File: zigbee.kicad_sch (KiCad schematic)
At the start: 17 parts, among them IC2 CC2652P1FRGZR, Y1 Crystal, Y2 Crystal_GND24

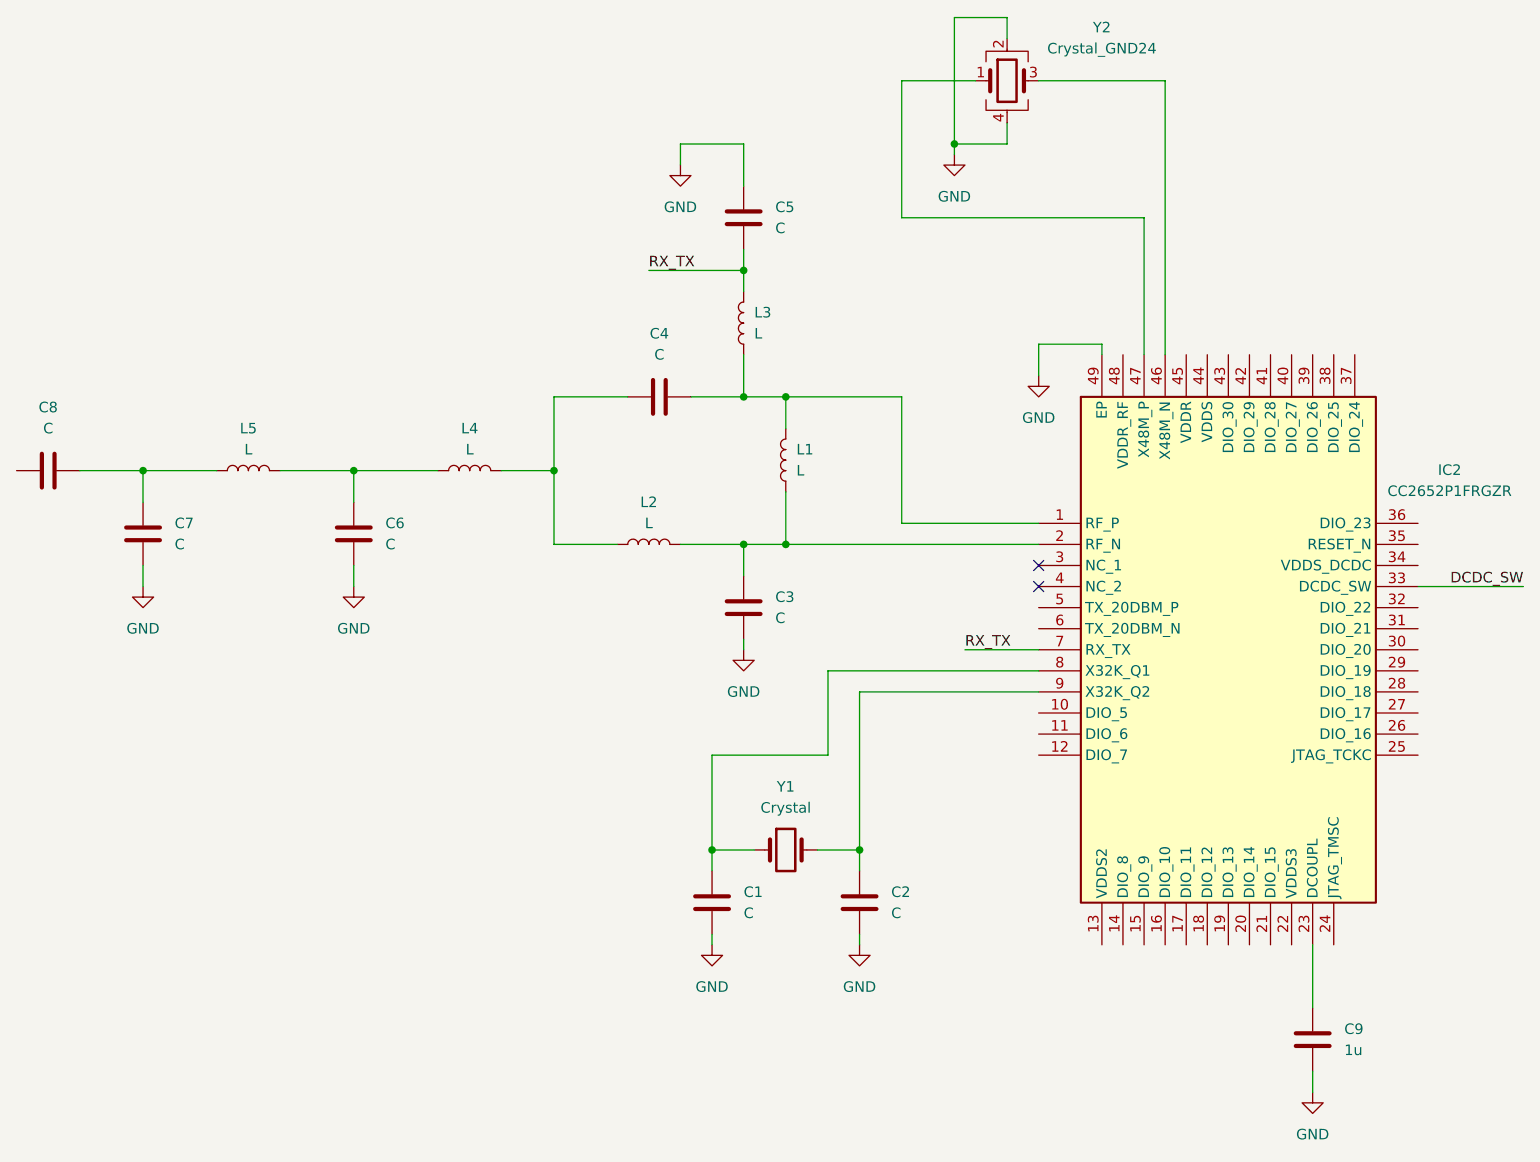
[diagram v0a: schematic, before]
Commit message: Started power circuitry and added more custom schematic symbols
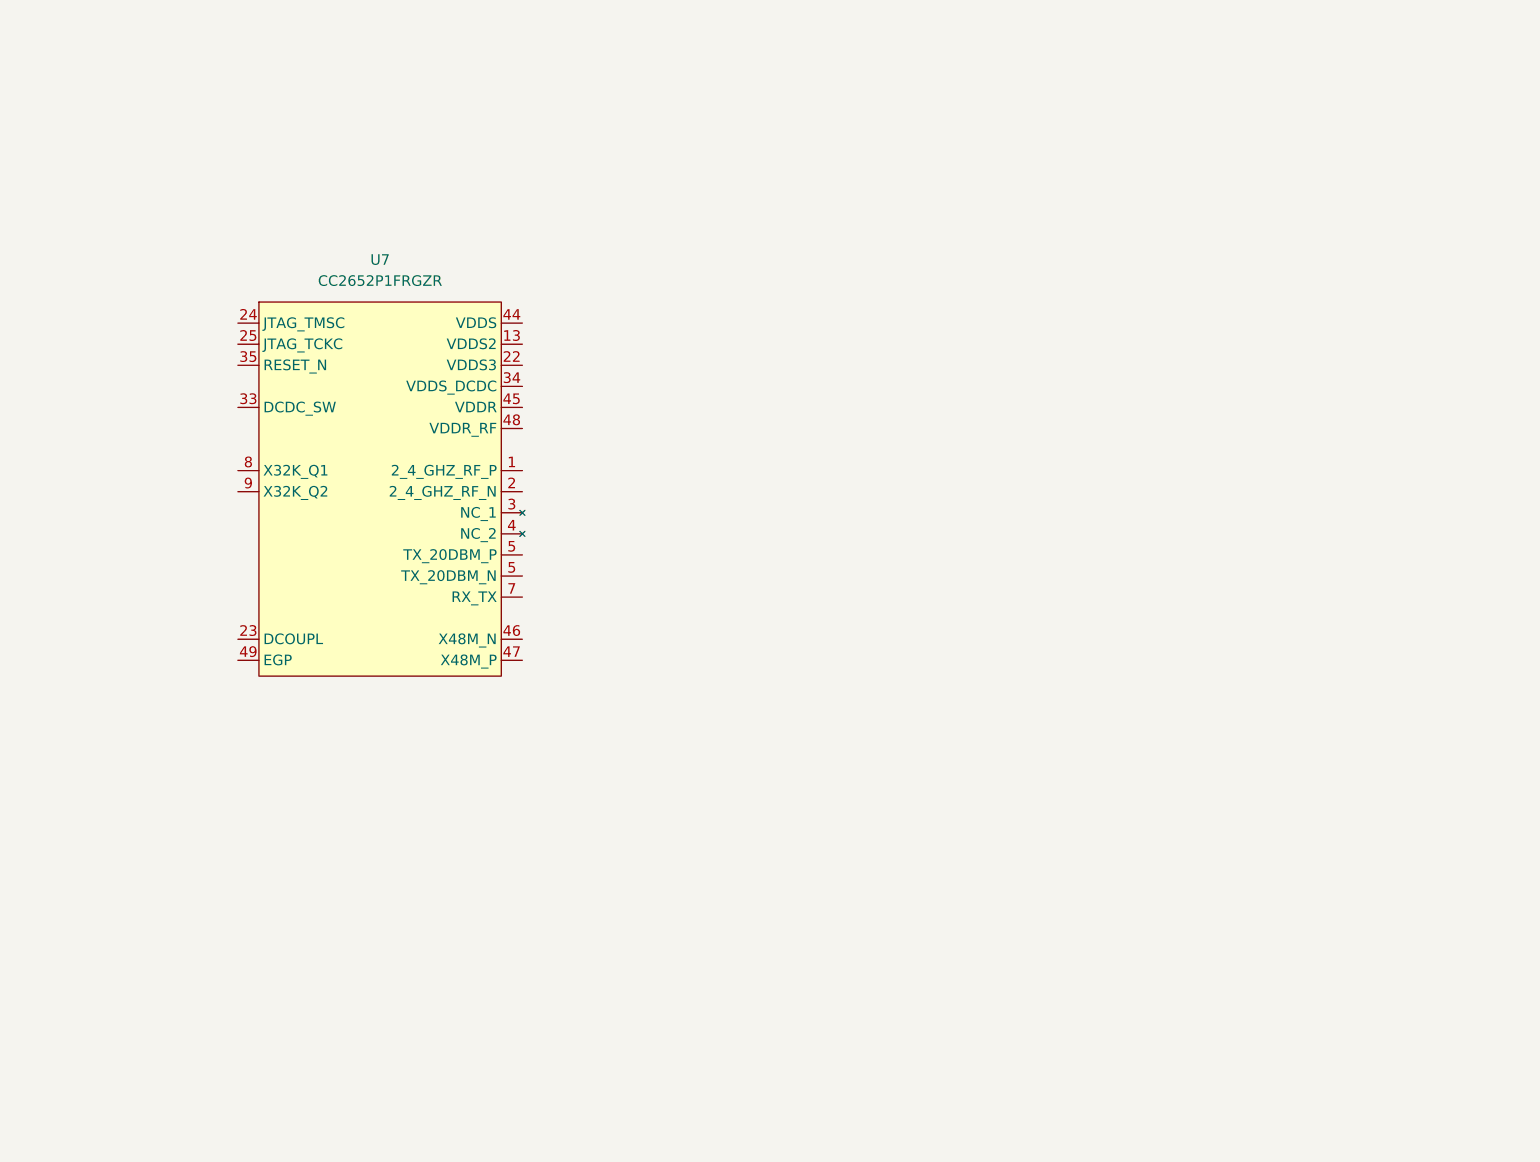
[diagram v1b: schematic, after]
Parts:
- removed C1, C2, C3, C4, C5, C6, C7, C8: C, symbol Device:C
- removed C9: 1u, symbol Device:C
- removed IC2: CC2652P1FRGZR, CC2652P1FRGZR:QFN50P700X700X100-49N-D, symbol CC2652P1FRGZR:CC2652P1FRGZR
- removed L1, L2, L3, L4, L5: L, symbol Device:L
- removed Y1: Crystal, symbol Device:Crystal
- removed Y2: Crystal_GND24, symbol Device:Crystal_GND24
- added U7: CC2652P1FRGZR, symbol SoftServicesSymbolLibrary:CC2652P1FRGZR
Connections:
- no-connect marks 2 -> 0

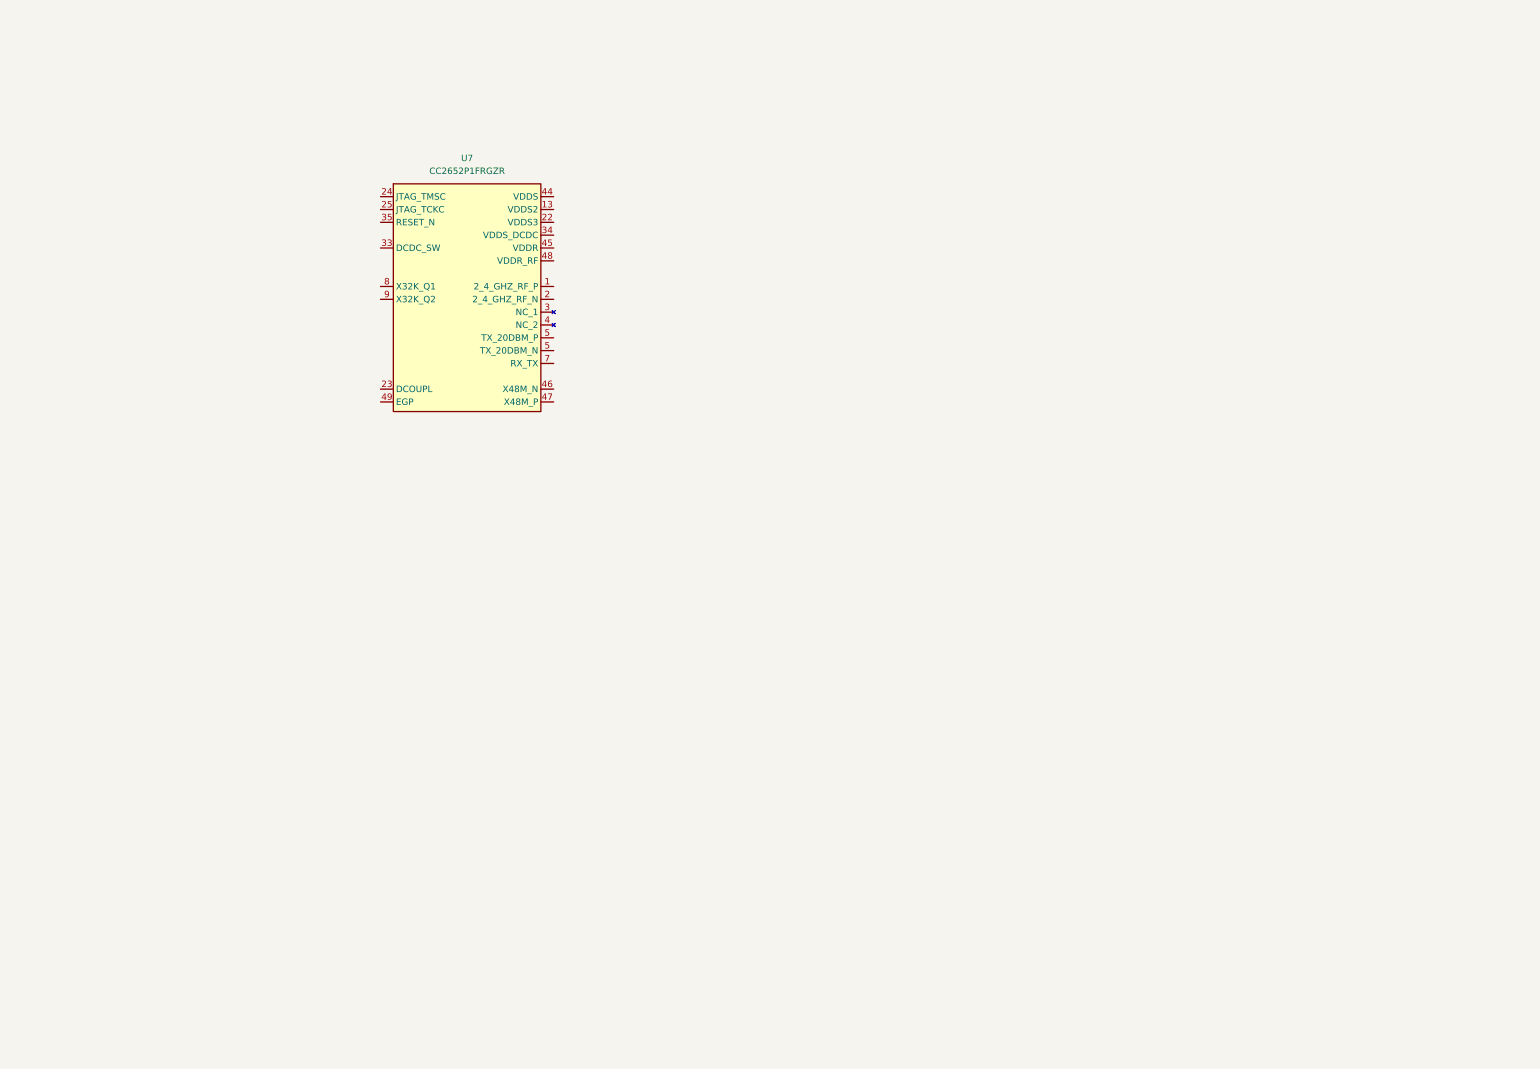
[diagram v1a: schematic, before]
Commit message: Finished CC2652P schematic
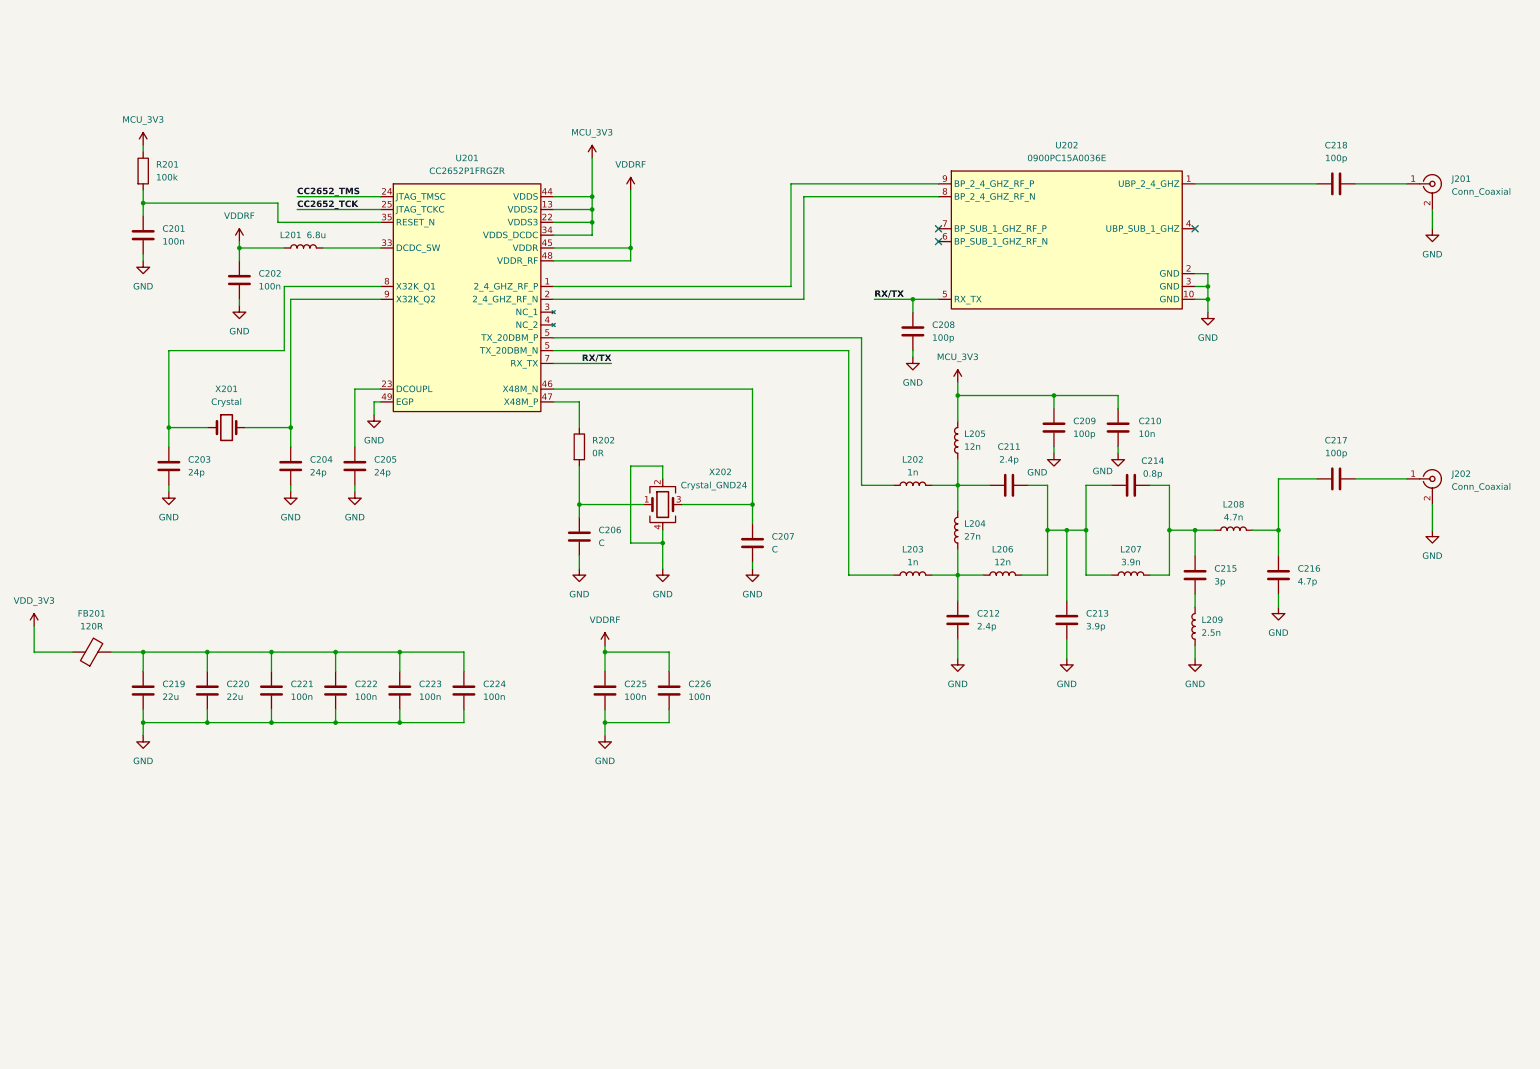
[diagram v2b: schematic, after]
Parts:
- added C201, C202, C221, C222, C223, C224, C225, C226: 100n, symbol Device:C
- added C203, C204, C205: 24p, symbol Device:C
- added C206, C207: C, symbol Device:C
- added C208, C209, C217, C218: 100p, symbol Device:C
- added C210: 10n, symbol Device:C
- added C211, C212: 2.4p, symbol Device:C
- added C213: 3.9p, symbol Device:C
- added C214: 0.8p, symbol Device:C
- added C215: 3p, symbol Device:C
- added C216: 4.7p, symbol Device:C
- added C219, C220: 22u, symbol Device:C
- added FB201: 120R, symbol Device:FerriteBead
- added J201, J202: Conn_Coaxial, symbol Connector:Conn_Coaxial
- added L201: 6.8u, symbol Device:L
- added L202, L203: 1n, symbol Device:L
- added L204: 27n, symbol Device:L
- added L205, L206: 12n, symbol Device:L
- added L207: 3.9n, symbol Device:L
- added L208: 4.7n, symbol Device:L
- added L209: 2.5n, symbol Device:L
- added R201: 100k, symbol Device:R
- added R202: 0R, symbol Device:R
- added U202: 0900PC15A0036E, symbol SoftServicesSymbolLibrary:0900PC15A0036E
- added X201: Crystal, symbol Device:Crystal
- added X202: Crystal_GND24, symbol Device:Crystal_GND24
- renumbered U7 to U201
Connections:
- net at U201.1 (2_4_GHZ_RF_P): now also U202.9 (BP_2_4_GHZ_RF_P)
- net MCU_3V3: now reaches U201.13 (VDDS2)
- net MCU_3V3: now also U201.22 (VDDS3), U201.34 (VDDS_DCDC), U201.44 (VDDS), C209.1, C210.1, L205.2, R201.1
- net at U201.2 (2_4_GHZ_RF_N): now also U202.8 (BP_2_4_GHZ_RF_N)
- net at U201.23 (DCOUPL): now also C205.1
- net CC2652_TMS: now reaches U201.24 (JTAG_TMSC)
- net CC2652_TCK: now reaches U201.25 (JTAG_TCKC)
- net at U201.33 (DCDC_SW): now also L201.2
- net at U201.35 (RESET_N): now also C201.1, R201.2
- net VDDRF: now reaches U201.45 (VDDR)
- net VDDRF: now also U201.48 (VDDR_RF), C202.1, C225.1, C226.1, L201.1
- net at U201.46 (X48M_N): now also C207.1, X202.3
- net at U201.47 (X48M_P): now also R202.1
- net GND: now reaches U201.49 (EGP)
- net GND: now also C201.2, C202.2, C203.2, C204.2, C205.2, C206.2, C207.2, C208.2, C209.2, C210.2, C212.2, C213.2, C216.1, C219.2, C220.2, C221.2, C222.2, C223.2, C224.2, C225.2, C226.2, J201.2 (Ext), J202.2 (Ext), L209.1, U202.10 (GND), U202.2 (GND), U202.3 (GND), X202.2, X202.4
- net at U201.5 (TX_20DBM_N): now also L203.1
- net RX/TX: now reaches U201.7 (RX_TX)
- net RX/TX: now also C208.1, U202.5 (RX_TX)
- net at U201.8 (X32K_Q1): now also C203.1, X201.1
- net at U201.9 (X32K_Q2): now also C204.1, X201.2
- new net: C218.1, J201.1 (In)
- new net: C214.2, C215.2, L207.2, L208.1
- new net: C216.2, C217.2, L208.2
- new net: L202.1, U201.5 (TX_20DBM_N)
- new net: C211.1, L202.2, L204.2, L205.1
- new net: C219.1, C220.1, C221.1, C222.1, C223.1, C224.1, FB201.2
- new net: C211.2, C213.1, C214.1, L206.2, L207.1
- new net: C212.1, L203.2, L204.1, L206.1
- new net: C206.1, R202.2, X202.1
- new net: C218.2, U202.1 (UBP_2_4_GHZ)
- new net: C217.1, J202.1 (In)
- new net: C215.1, L209.2
- new net VDD_3V3: FB201.1
- no-connect marks 0 -> 3

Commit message: Fixed schematic symbol errors
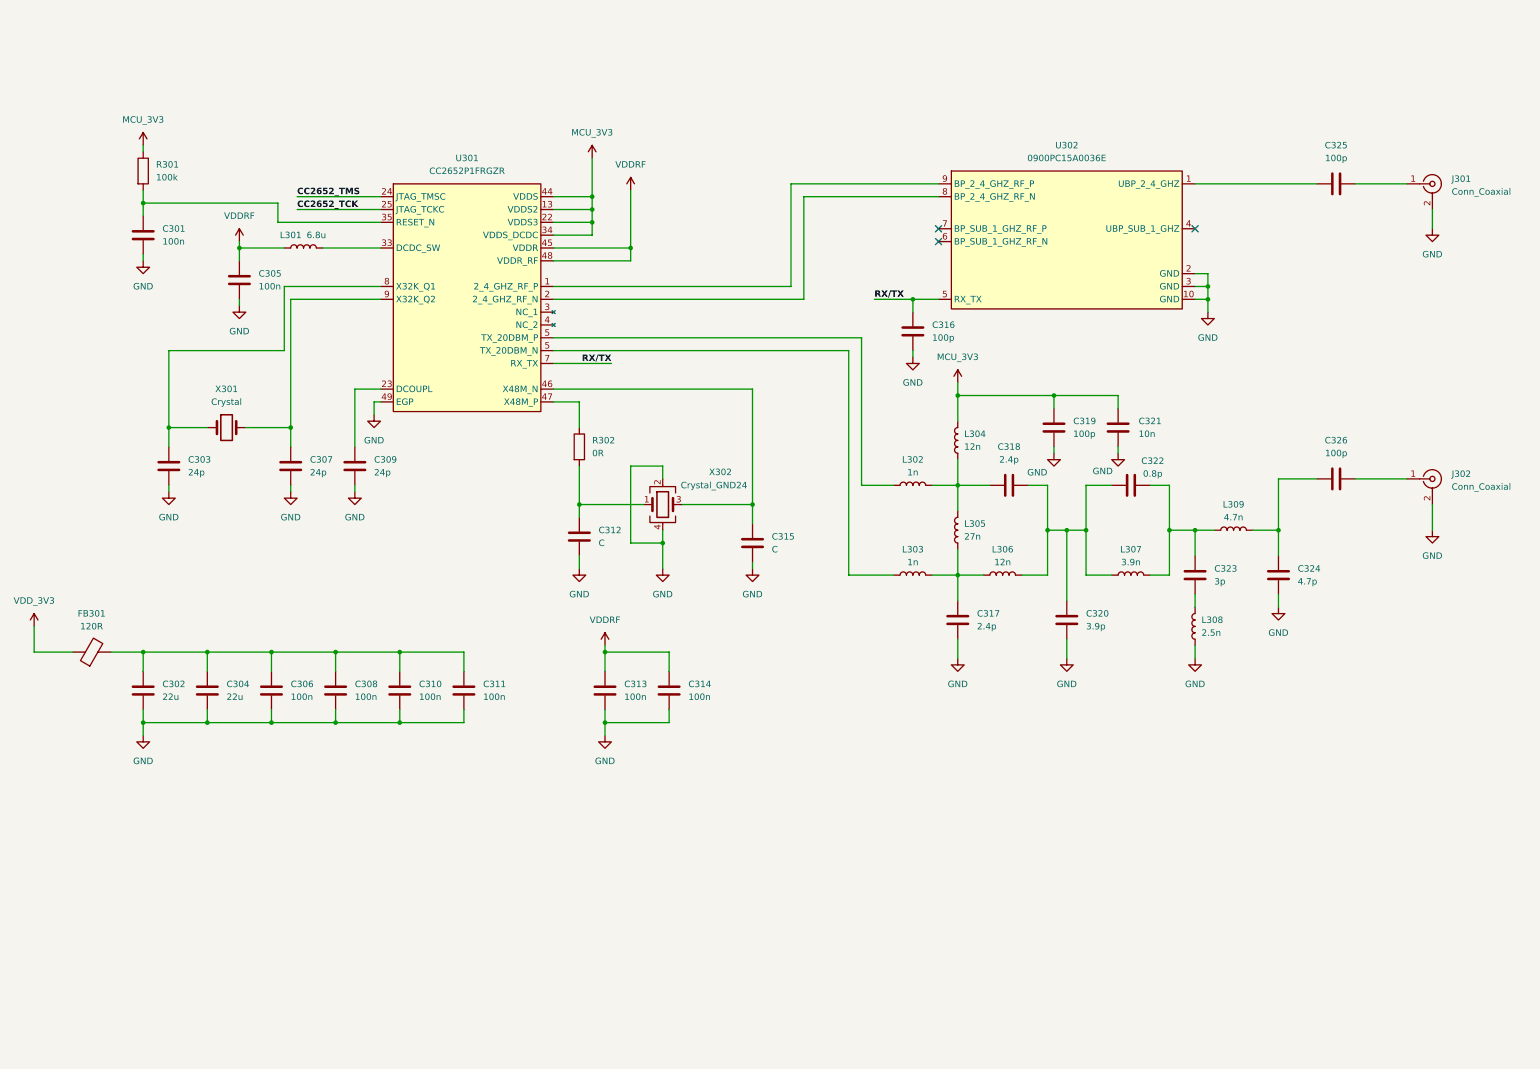
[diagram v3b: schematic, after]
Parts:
- renumbered C201 to C301, C219 to C302, C203 to C303, C220 to C304, C202 to C305, C221 to C306, C204 to C307, C222 to C308, C205 to C309, C223 to C310, C224 to C311, C206 to C312, C225 to C313, C226 to C314, C207 to C315, C208 to C316, C212 to C317, C211 to C318, C209 to C319, C213 to C320, C210 to C321, C214 to C322, C215 to C323, C216 to C324, C218 to C325, C217 to C326, FB201 to FB301, J201 to J301, J202 to J302, L201 to L301, L202 to L302, L203 to L303, L205 to L304, L204 to L305, L206 to L306, L207 to L307, L209 to L308, L208 to L309, R201 to R301, R202 to R302, U201 to U301, U202 to U302, X201 to X301, X202 to X302
